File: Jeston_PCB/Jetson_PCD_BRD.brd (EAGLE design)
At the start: 87 x 50 mm, 4 parts, among them Q2 NTD3055L104G

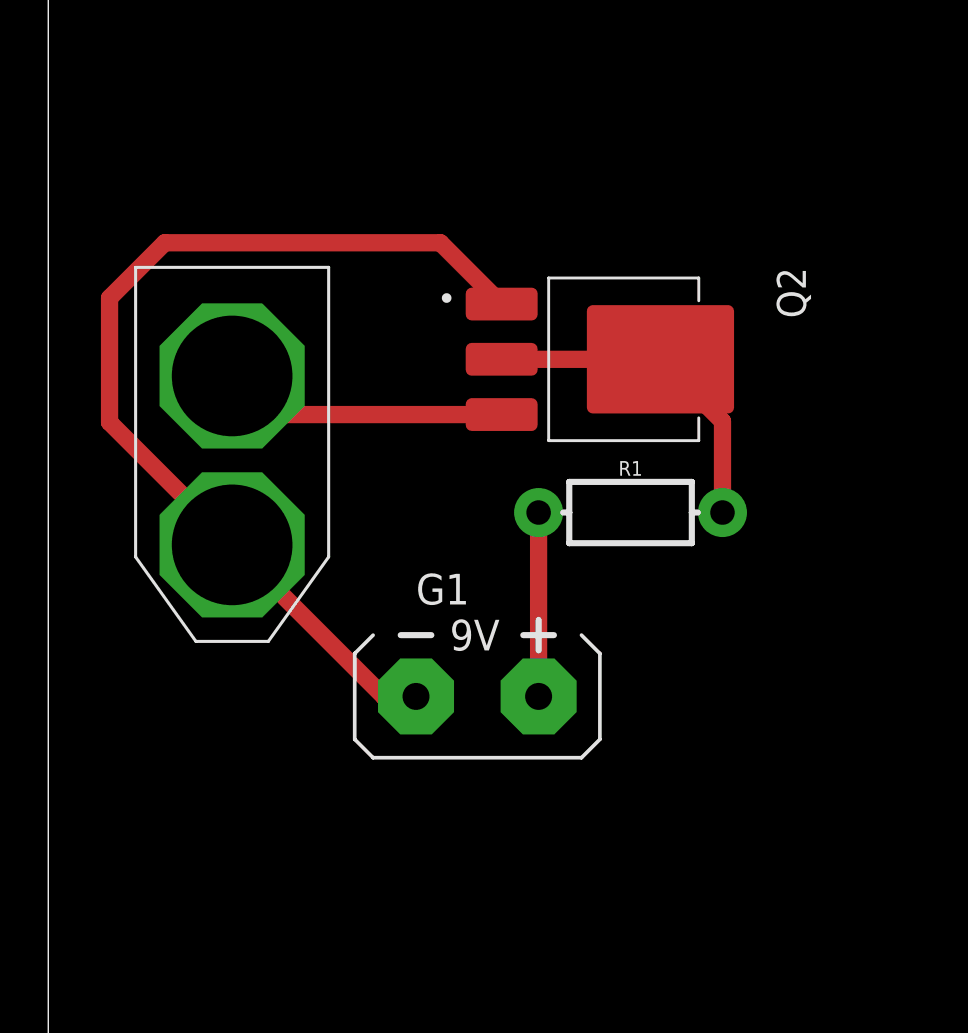
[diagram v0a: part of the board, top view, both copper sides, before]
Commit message: replaced battery port with XT60
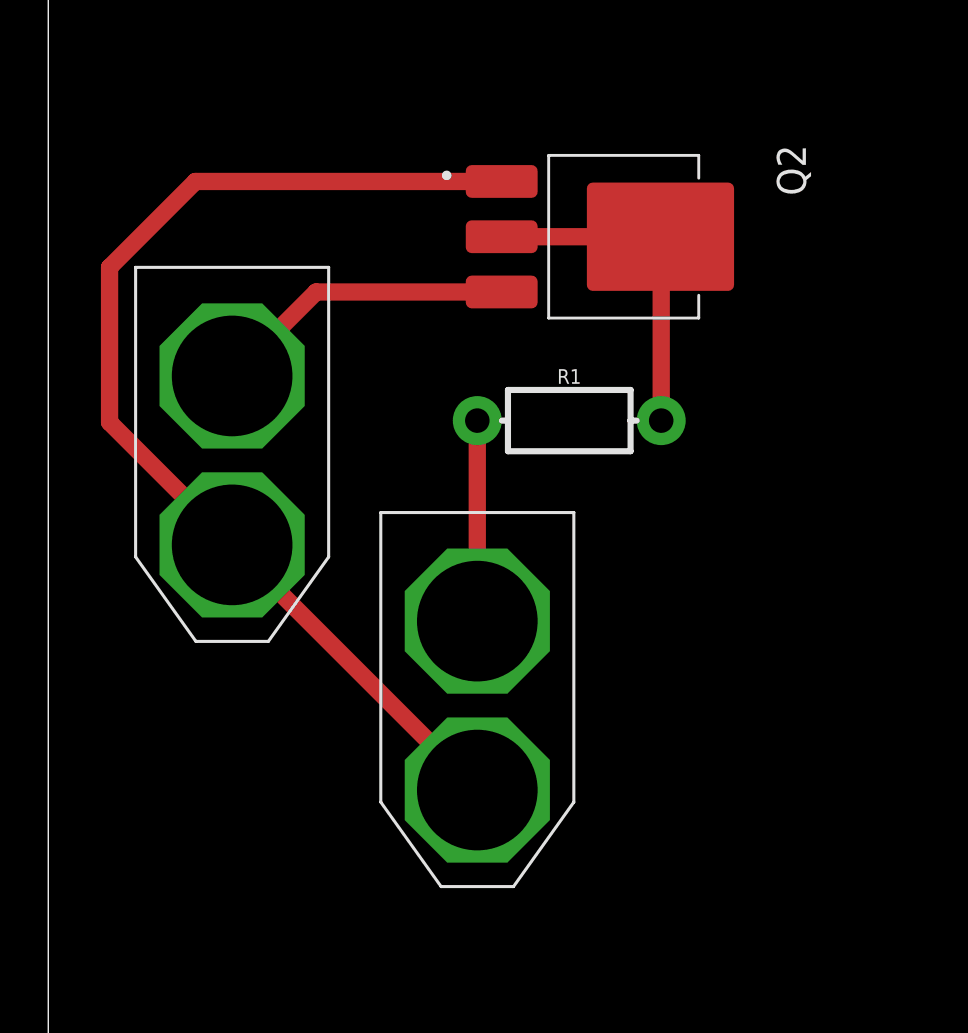
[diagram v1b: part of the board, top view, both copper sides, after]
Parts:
- removed G1: AB9V, battery:AB9V
- added U$2: XT60, XT60:XT60
- moved Q2 5.08 mm to (22.9, 34.3)
- moved R1 4.58 mm to (21.6, 26.7)
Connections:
- net N$1: now also U$2.-; no longer G1.-
- net N$2: now also U$2.+; no longer G1.+
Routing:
- net N$1: track 40.8 -> 45.7 mm
- net N$4: track 11.8 -> 12.6 mm
- net N$2: track 7.62 -> 8.31 mm
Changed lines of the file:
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@@
 </autorouter>
 <elements>
-<element name="G1" library="battery" library_urn="urn:adsk.eagle:library:109" package="AB9V" package3d_urn="urn:adsk.eagle:package:4600/1" value="AB9V" x="17.78" y="15.24" smashed="yes" rot="R270">
-<attribute name="NAME" x="15.24" y="19.05" size="1.27" layer="25" ratio="10"/>
-<attribute name="POPULARITY" value="32" x="11.43" y="-17.78" size="1.778" layer="27" rot="R270" display="off"/>
-<attribute name="VALUE" x="15.24" y="10.795" size="1.27" layer="27" ratio="10"/>
+<element name="Q2" library="Transistor" library_urn="urn:adsk.eagle:library:11396518" package="DPAK4" package3d_urn="urn:adsk.eagle:package:10893256/2" value="NTD3055L104G" x="22.86" y="34.29" smashed="yes" rot="R270">
+<attribute name="CREATED_BY" value="PCBLayout.com" x="12.7" y="11.43" size="1.778" layer="27" rot="R270" display="off"/>
+<attribute name="MANUFACTURER" value="ON SEMICONDUCTORS" x="12.7" y="11.43" size="1.778" layer="27" rot="R270" display="off"/>
+<attribute name="MPN" value="NTD3055L104G" x="12.7" y="11.43" size="1.778" layer="27" rot="R270" display="off"/>
+<attribute name="NAME" x="30.1975" y="38.1" size="1.2" layer="25" ratio="10" rot="R270"/>
+<attribute name="PACKAGE" value="DPAK-4" x="12.7" y="11.43" size="1.778" layer="27" rot="R270" display="off"/>
+<attribute name="VALUE" x="13.97" y="38.1" size="1.2" layer="27" ratio="10" rot="R270"/>
 </element>
-<element name="Q2" library="Transistor" library_urn="urn:adsk.eagle:library:11396518" package="DPAK4" package3d_urn="urn:adsk.eagle:package:10893256/2" value="NTD3055L104G" x="22.86" y="29.21" smashed="yes" rot="R270">
-<attribute name="CREATED_BY" value="PCBLayout.com" x="12.7" y="6.35" size="1.778" layer="27" rot="R270" display="off"/>
-<attribute name="MANUFACTURER" value="ON SEMICONDUCTORS" x="12.7" y="6.35" size="1.778" layer="27" rot="R270" display="off"/>
-<attribute name="MPN" value="NTD3055L104G" x="12.7" y="6.35" size="1.778" layer="27" rot="R270" display="off"/>
-<attribute name="NAME" x="30.1975" y="33.02" size="1.2" layer="25" ratio="10" rot="R270"/>
-<attribute name="PACKAGE" value="DPAK-4" x="12.7" y="6.35" size="1.778" layer="27" rot="R270" display="off"/>
-<attribute name="VALUE" x="13.97" y="33.02" size="1.2" layer="27" ratio="10" rot="R270"/>
-</element>
-<element name="R1" library="SparkFun-Resistors" package="AXIAL-0.3-KIT" value=" " x="24.13" y="22.86" smashed="yes">
-<attribute name="NAME" x="24.13" y="24.384" size="0.6096" layer="25" font="vector" ratio="20" align="bottom-center"/>
-<attribute name="PROD_ID" value=" " x="41.91" y="-13.97" size="1.778" layer="27" display="off"/>
-<attribute name="VALUE" x="24.13" y="21.336" size="0.6096" layer="27" font="vector" ratio="20" align="top-center"/>
+<element name="R1" library="SparkFun-Resistors" package="AXIAL-0.3-KIT" value=" " x="21.59" y="26.67" smashed="yes">
+<attribute name="NAME" x="21.59" y="28.194" size="0.6096" layer="25" font="vector" ratio="20" align="bottom-center"/>
+<attribute name="PROD_ID" value=" " x="39.37" y="-10.16" size="1.778" layer="27" display="off"/>
+<attribute name="VALUE" x="22.86" y="25.146" size="0.6096" layer="27" font="vector" ratio="20" align="top-center"/>
 </element>
 <element name="U$1" library="XT60" package="XT60" value="XT60" x="7.62" y="33.02" smashed="yes" rot="R270"/>
+<element name="U$2" library="XT60" package="XT60" value="XT60" x="17.78" y="22.86" smashed="yes" rot="R270"/>
 </elements>
 <signals>
 <signal name="N$1">
-<contactref element="G1" pad="-"/>
 <contactref element="Q2" pad="1"/>
 <contactref element="U$1" pad="-"/>
-<wire x1="16.25" y1="34.04" x2="18.79" y2="31.5" width="0.71628125" layer="1"/>
-<wire x1="16.25" y1="34.04" x2="4.83" y2="34.04" width="0.71628125" layer="1"/>
-<wire x1="2.54" y1="31.75" x2="4.83" y2="34.04" width="0.71628125" layer="1"/>
-<wire x1="2.54" y1="31.75" x2="2.54" y2="26.6" width="0.71628125" layer="1"/>
+<wire x1="18.79" y1="36.58" x2="6.1" y2="36.58" width="0.71628125" layer="1"/>
+<wire x1="2.54" y1="33.02" x2="6.1" y2="36.58" width="0.71628125" layer="1"/>
+<wire x1="2.54" y1="33.02" x2="2.54" y2="26.6" width="0.71628125" layer="1"/>
 <wire x1="2.54" y1="26.6" x2="7.585" y2="21.555" width="0.71628125" layer="1"/>
 <wire x1="7.585" y1="21.555" x2="7.62" y2="21.52" width="0.1524" layer="1"/>
-<wire x1="15.24" y1="15.24" x2="13.9" y2="15.24" width="0.71628125" layer="1"/>
-<wire x1="13.9" y1="15.24" x2="7.62" y2="21.52" width="0.71628125" layer="1"/>
+<wire x1="17.78" y1="11.36" x2="7.62" y2="21.52" width="0.71628125" layer="1"/>
+<contactref element="U$2" pad="-"/>
 </signal>
 <signal name="N$2">
-<contactref element="G1" pad="+"/>
 <contactref element="R1" pad="P$1"/>
-<wire x1="20.32" y1="22.86" x2="20.32" y2="15.24" width="0.71628125" layer="1"/>
+<contactref element="U$2" pad="+"/>
+<wire x1="17.78" y1="26.67" x2="17.78" y2="18.36" width="0.71628125" layer="1"/>
 </signal>
 <signal name="N$3">
@@
 <contactref element="Q2" pad="2"/>
 <contactref element="Q2" pad="4"/>
-<wire x1="18.79" y1="29.21" x2="25.37" y2="29.21" width="0.71628125" layer="1"/>
-<wire x1="27.94" y1="22.86" x2="27.94" y2="26.64" width="0.71628125" layer="1"/>
-<wire x1="27.94" y1="26.64" x2="25.37" y2="29.21" width="0.71628125" layer="1"/>
+<wire x1="25.37" y1="34.29" x2="18.79" y2="34.29" width="0.71628125" layer="1"/>
+<wire x1="25.4" y1="26.67" x2="25.4" y2="34.26" width="0.71628125" layer="1"/>
+<wire x1="25.4" y1="34.26" x2="25.37" y2="34.29" width="0.71628125" layer="1"/>
 </signal>
 <signal name="N$4">
 <contactref element="Q2" pad="3"/>
 <contactref element="U$1" pad="+"/>
-<wire x1="7.62" y1="28.52" x2="9.22" y2="26.92" width="0.71628125" layer="1"/>
-<wire x1="9.22" y1="26.92" x2="18.79" y2="26.92" width="0.71628125" layer="1"/>
+<wire x1="18.79" y1="32" x2="11.1" y2="32" width="0.71628125" layer="1"/>
+<wire x1="7.62" y1="28.52" x2="11.1" y2="32" width="0.71628125" layer="1"/>
 </signal>
 </signals>
